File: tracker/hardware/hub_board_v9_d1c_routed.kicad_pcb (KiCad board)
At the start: 4 copper layers, 103 x 103 mm, 44 parts, among them U1 ESP32-S3-WROOM-1U-N8R8, U2 LoRa2021F33-2G4, U3 LoRa2021_Castellated, U4 SX1280, U5 MAX-M10S, U6 MS5611-01BA, U7 TPS7A02

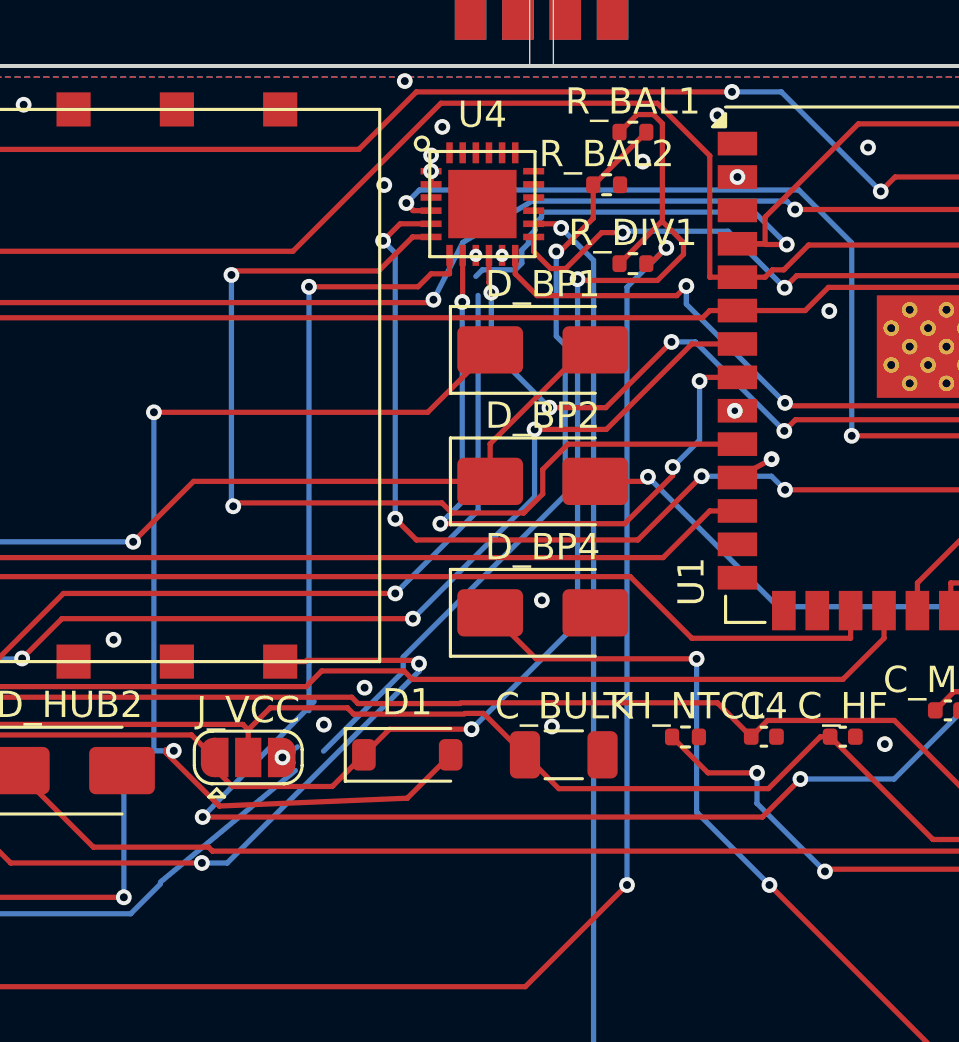
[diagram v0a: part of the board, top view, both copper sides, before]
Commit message: feat(pcb): v25 -- Astra ladder #1 worked: clearance 8->6, total 111 (BEST)
Two refutations first, both honest and measured:
  v23 (relocate anchoring via): no position clears the full local clearance
    graph even at exactly 0.20mm -> B.Cu there is structurally over-constrained.
  v24 (move segment to In2.Cu): In2 has barrels there too (0.1938 / 0.1450 vs
    0.30 needed).
  v25 (Astra ladder #1 = reroute the escape on the same layer): WORKED.
    A* on a 0.125mm grid with the complete obstacle set (foreign tracks 0.40
    centre, ALL through-via barrels 0.60 centre, pads 0.30 edge), endpoints
    exact so connectivity is preserved: 2 segments rerouted (16 verts/15.4mm
    and 18 verts/7.0mm).

BOARD OF RECORD: shorts 0 | crossings 0 | via/hole/annular 0 | clearance 6
| unconnected 26 | total 111.

Remaining clearance 6:
  5 via-in-pad NEIGHBOURS (0.125/0.150) -- Astra: IPC-4761 fill-and-cap does
    NOT waive copper clearance; requires a documented exception TABLE with
    JLCPCB written confirmation per pair.
  1 track-track /F33_SCK vs /I2C_SCL 0.1648 -- fixable (I2C is a slow bus
    with unlimited detour tolerance); target of v26.

Unconnected 26 = the documented classes (wing interface J_W1..J_W4 +
W*_SOLAR_N + CUT_SENSE_W*, same-net zone/via pairs, 1 F33_SCK residual); the
+1 vs v22 is a 3-for-2 re-pairing of the SAME wing-interface class, not new
missing copper.
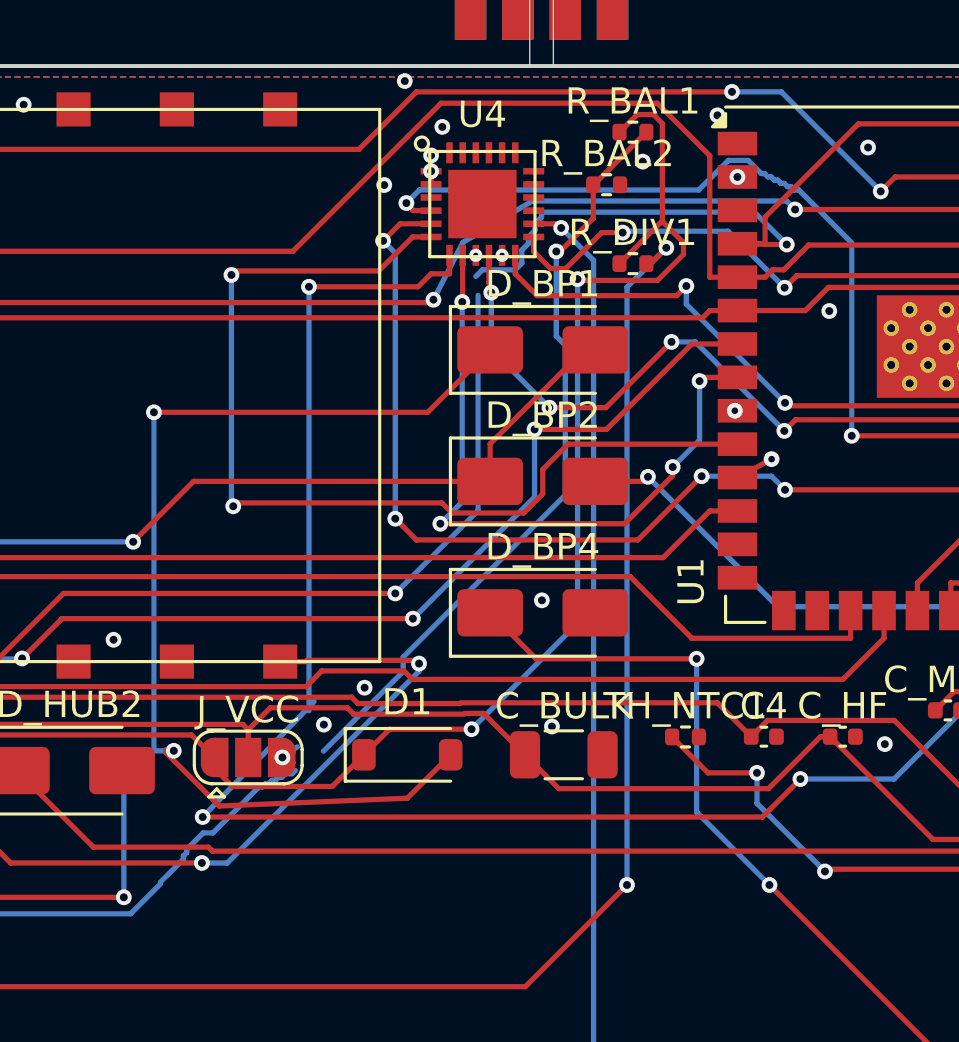
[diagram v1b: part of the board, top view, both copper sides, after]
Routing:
- net /SX1280_RESET_N: track 39.9 -> 40.8 mm
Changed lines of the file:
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@@
+	)
+	(segment
+		(start 41.1299 27.289974)
+		(end 41.2549 27.164974)
+		(width 0.2)
+		(layer "B.Cu")
+		(net 30)
+	)
+	(segment
+		(start 38.6299 29.164974)
+		(end 39.0049 29.164974)
+		(width 0.2)
+		(layer "B.Cu")
+		(net 30)
+	)
+	(segment
+		(start 38.0049 29.789974)
+		(end 38.6299 29.164974)
+		(width 0.2)
+		(layer "B.Cu")
+		(net 30)
+	)
+	(segment
+		(start 38.0049 29.914974)
+		(end 38.0049 29.789974)
+		(width 0.2)
+		(layer "B.Cu")
+		(net 30)
 	)
 	(segment
@@
 	)
 	(segment
+		(start 41.3799 27.164974)
+		(end 41.5049 27.039974)
+		(width 0.2)
+		(layer "B.Cu")
+		(net 30)
+	)
+	(segment
+		(start 41.2549 27.164974)
+		(end 41.3799 27.164974)
+		(width 0.2)
+		(layer "B.Cu")
+		(net 30)
+	)
+	(segment
 		(start 42.147064 25.941063)
 		(end 42.217125 25.891673)
@@
 	)
 	(segment
+		(start 39.0049 29.164974)
+		(end 40.7549 27.414974)
+		(width 0.2)
+		(layer "B.Cu")
+		(net 30)
+	)
+	(segment
 		(start 52.4027 16.3118)
 		(end 52.4027 10.617)
@@
 	)
 	(segment
+		(start 37.8799 30.164974)
+		(end 37.8799 30.039974)
+		(width 0.2)
+		(layer "B.Cu")
+		(net 30)
+	)
+	(segment
 		(start 20.7925 30.2925)
 		(end 22.7384 32.2384)
@@
 	)
 	(segment
+		(start 40.7549 27.414974)
+		(end 40.8799 27.414974)
+		(width 0.2)
+		(layer "B.Cu")
+		(net 30)
+	)
+	(segment
+		(start 41.0049 27.289974)
+		(end 41.1299 27.289974)
+		(width 0.2)
+		(layer "B.Cu")
+		(net 30)
+	)
+	(segment
+		(start 41.6299 27.039974)
+		(end 41.7549 26.914974)
+		(width 0.2)
+		(layer "B.Cu")
+		(net 30)
+	)
+	(segment
+		(start 42.0049 26.914974)
+		(end 42.139974 26.789974)
+		(width 0.2)
+		(layer "B.Cu")
+		(net 30)
+	)
+	(segment
+		(start 40.8799 27.414974)
+		(end 41.0049 27.289974)
+		(width 0.2)
+		(layer "B.Cu")
+		(net 30)
+	)
+	(segment
+		(start 41.7549 26.914974)
+		(end 42.0049 26.914974)
+		(width 0.2)
+		(layer "B.Cu")
+		(net 30)
+	)
+	(segment
 		(start 37.0049 31.035)
-		(end 42.139974 26.789974)
+		(end 37.8799 30.164974)
+		(width 0.2)
+		(layer "B.Cu")
+		(net 30)
+	)
+	(segment
+		(start 37.8799 30.039974)
+		(end 38.0049 29.914974)
+		(width 0.2)
+		(layer "B.Cu")
+		(net 30)
+	)
+	(segment
+		(start 41.5049 27.039974)
+		(end 41.6299 27.039974)
 		(width 0.2)
 		(layer "B.Cu")
@@
 	)
 	(segment
+		(start 57.4817 4.7138)
+		(end 58.6067 3.5888)
+		(width 0.2)
+		(layer "B.Cu")
+		(net 39)
+	)
+	(segment
+		(start 60.1067 4.2138)
+		(end 60.2317 4.2138)
+		(width 0.2)
+		(layer "B.Cu")
+		(net 39)
+	)
+	(segment
+		(start 61.1067 4.7138)
+		(end 61.2852 4.7138)
+		(width 0.2)
+		(layer "B.Cu")
+		(net 39)
+	)
+	(segment
+		(start 59.3567 3.5888)
+		(end 59.8567 4.0888)
+		(width 0.2)
+		(layer "B.Cu")
+		(net 39)
+	)
+	(segment
+		(start 59.8567 4.0888)
+		(end 59.9817 4.0888)
+		(width 0.2)
+		(layer "B.Cu")
+		(net 39)
+	)
+	(segment
+		(start 60.8567 4.5888)
+		(end 60.9817 4.5888)
+		(width 0.2)
+		(layer "B.Cu")
+		(net 39)
+	)
+	(segment
+		(start 59.9817 4.0888)
+		(end 60.1067 4.2138)
+		(width 0.2)
+		(layer "B.Cu")
+		(net 39)
+	)
+	(segment
+		(start 60.6067 4.4638)
+		(end 60.7317 4.4638)
+		(width 0.2)
+		(layer "B.Cu")
+		(net 39)
+	)
+	(segment
+		(start 60.4817 4.3388)
+		(end 60.6067 4.4638)
+		(width 0.2)
+		(layer "B.Cu")
+		(net 39)
+	)
+	(segment
+		(start 60.9817 4.5888)
+		(end 61.1067 4.7138)
+		(width 0.2)
+		(layer "B.Cu")
+		(net 39)
+	)
+	(segment
 		(start 46.3592 5.2113)
 		(end 46.8567 4.7138)
@@
 	)
 	(segment
+		(start 60.7317 4.4638)
+		(end 60.8567 4.5888)
+		(width 0.2)
+		(layer "B.Cu")
+		(net 39)
+	)
+	(segment
+		(start 60.3567 4.3388)
+		(end 60.4817 4.3388)
+		(width 0.2)
+		(layer "B.Cu")
+		(net 39)
+	)
+	(segment
 		(start 63.2965 6.7251)
 		(end 63.2965 14.0633)
@@
 	)
 	(segment
+		(start 60.2317 4.2138)
+		(end 60.3567 4.3388)
+		(width 0.2)
+		(layer "B.Cu")
+		(net 39)
+	)
+	(segment
+		(start 46.8567 4.7138)
+		(end 57.4817 4.7138)
+		(width 0.2)
+		(layer "B.Cu")
+		(net 39)
+	)
+	(segment
 		(start 61.2852 4.7138)
 		(end 63.2965 6.7251)
@@
 	)
 	(segment
-		(start 46.8567 4.7138)
-		(end 61.2852 4.7138)
-		(width 0.2)
-		(layer "B.Cu")
+		(start 58.6067 3.5888)
+		(end 59.3567 3.5888)
+		(width 0.2)
+		(layer "B.Cu")
